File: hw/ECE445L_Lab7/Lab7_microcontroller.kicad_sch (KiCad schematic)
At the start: 12 parts, among them J4 Debugger, SW6 RST, U4 M0G3507QDGS32RQ1, Y1 16MHz

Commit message: work on schem
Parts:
- removed C4: 10nF, ECE445L:C_Radial_100mil, symbol ECE445L:C
- removed R3: 47k, ECE445L:R_Axial_DIN0204_L3.6mm_D1.6mm_P7.62mm_Horizontal, symbol ECE445L:R_0.125W
- removed R7: 100k, ECE445L:R_Axial_DIN0204_L3.6mm_D1.6mm_P7.62mm_Horizontal, symbol ECE445L:R_0.125W
- removed SW6: RST, ECE445L:SW_PUSH_6mm, symbol ECE445L:SW_Push
- added C13, C14: 10pF, Capacitor_SMD:C_0201_0603Metric_Pad0.64x0.40mm_HandSolder, symbol ECE445L:C
- added C_{b,3}: 0.1uF, ECE445L:C_Radial_100mil, symbol ECE445L:C
- added C_{b,4}: 10uF, ECE445L:C_Radial_100mil, symbol ECE445L:C
- added C_{core,2}: 0.47uF, Capacitor_SMD:C_0201_0603Metric_Pad0.64x0.40mm_HandSolder, symbol ECE445L:C
- added J_{flash,2}: Debugger, ECE445L:PinHeader_1x04_P2.54mm_Vertical, symbol ECE445L:Header_4
- added J_{test}: Conn_02x04_Counter_Clockwise, Connector_PinSocket_2.54mm:PinSocket_2x04_P2.54mm_Vertical, symbol Connector_Generic:Conn_02x04_Counter_Clockwise
- added U6: M0G3507QDGS32RQ1, ECE445L:VSSOP_0.5mm_32pin_handsolder, symbol ECE445L:M0G3507QDGS32RQ1
- added Y2: 16MHz, ECE445L:ABM3, symbol ECE445L:ABM3-16.000MHZ-B2-T
- C10, C11: footprint ECE445L:C_Radial_100mil -> Capacitor_SMD:C_0201_0603Metric_Pad0.64x0.40mm_HandSolder
- C_{core,1}: renamed from C9; footprint ECE445L:C_Radial_100mil -> Capacitor_SMD:C_0201_0603Metric_Pad0.64x0.40mm_HandSolder
- renumbered C8 to C_{b,1}, C7 to C_{b,2}, J4 to J_{flash,1}
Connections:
- net +3V3: now also C_{b,3}.1, C_{b,4}.1, J_{flash,2}.4 (C), U6.7 (VDD)
- net GND: now also C13.2, C14.2, C_{b,3}.2, C_{b,4}.2, C_{core,2}.2, J_{flash,2}.3 (C), J_{test}.4 (Pin_4), J_{test}.5 (Pin_5), U6.8 (VSS)
- net PA0 renamed uC_{1} - PA0
- net PA1 renamed uC_{1} - PA1
- net PA10: no longer names the net of U4.17 (PA10/CLK_OUT)
- net PA10: now also U6.16 (PA9/RTC_OUT/CLK_OUT)
- net PA11/SPI0_SCK renamed uC_{1} - PA11
- net PA12 renamed uC_{1} - PA12
- net PA13/TFT_D/C renamed uC_{1} - PA13
- net PA14/SPI0_PICO: no longer names the net of U4.21 (PA14/CLK_OUT/A0_12)
- net PA14/SPI0_PICO: now also U6.11 (PA4/LFCLK_IN/LFXOUT)
- net PA15/DACOUT renamed uC_{1} - PA15
- net PA16/SPI1_POCI renamed uC_{1} - PA16
- net uC_{1} - PA16: now also J_{test}.2 (Pin_2)
- net PA17/SPI1_CLK renamed uC_{1} - PA17
- net PA18/SPI1_PICO renamed uC_{1} - PA18
- net PA2 renamed uC_{1} - PA2
- net PA21 renamed uC_{1} - PA21
- net PA22 renamed uC_{1} - PA22
- net PA23 renamed uC_{1} - PA23
- net PA24/TFT_RESET renamed uC_{1} - PA24
- net PA25/SPI1_CS3 renamed uC_{1} - PA25
- net PA26 renamed uC_{1} - PA26
- net PA27/SPI1_CS1 renamed uC_{1} - PA27
- net uC_{1} - PA27: now also J_{test}.1 (Pin_1)
- net PA3 renamed uC_{1} - PA3
- net PA4 renamed uC_{1} - PA4
- net PA5/HFXIN renamed uC_{1} - HFXIN
- net uC_{1} - HFXIN: now also C13.1, Y2.1
- net PA6/HFXOUT renamed uC_{1} - HFXOUT
- net uC_{1} - HFXOUT: now also C14.1, Y2.2
- net PA7 renamed uC_{1} - PA7
- net PA8/SPI0_CS0 renamed uC_{1} - PA8
- net PA9 renamed uC_{1} - PA9
- net SWCLK: no longer names the net of J_{flash,1}.2 (B), U4.27 (PA20/SWCLK)
- net SWDIO: no longer names the net of J_{flash,1}.1 (A), U4.26 (PA19/SWDIO)
- new net: J_{flash,2}.1 (A), U6.26 (PA19/SWDIO)
- new net: J_{flash,2}.2 (B), U6.27 (PA20/SWCLK)
- new net: C_{core,2}.1, U6.3 (VCORE)
- new net uC_{2} - HFXIN: U6.12 (PA5/HFXIN/FCC_IN)
- new net uC_{2} - HFXOUT: U6.13 (PA6/HFCLK_IN/HFXOUT)
- new net uC_{2} - PA10: U6.17 (PA10/CLK_OUT)
- new net uC_{2} - PA11: U6.18 (PA11)
- new net uC_{2} - PA12: U6.19 (PA12/FCC_IN)
- new net uC_{2} - PA13: U6.20 (PA13)
- new net uC_{2} - PA14: J_{test}.6 (Pin_6), U6.21 (PA14/CLK_OUT/A0_12)
- new net uC_{2} - PA15: U6.22 (PA15/A1_0/DACOUT)
- new net uC_{2} - PA16: U6.23 (PA16/A1_1/FCC_IN)
- new net uC_{2} - PA17: U6.24 (PA17/A1_2)
- new net uC_{2} - PA18: U6.25 (PA18/A1_3)
- new net uC_{2} - PA2: U6.9 (PA2/ROSC)
- new net uC_{2} - PA21: J_{test}.7 (Pin_7), U6.28 (PA21/A1_7/VREF-)
- new net uC_{2} - PA22: J_{test}.8 (Pin_8), U6.29 (PA22/CLK_OUT/A0_7)
- new net uC_{2} - PA23: U6.30 (PA23/VREF+)
- new net uC_{2} - PA24: U6.31 (PA24/A0_3)
- new net uC_{2} - PA25: U6.32 (PA25/A0_2)
- new net uC_{2} - PA26: U6.1 (PA26/A0_1)
- new net uC_{2} - PA27: U6.2 (PA27/RTC_OUT/A0_0)
- new net uC_{2} - PA3: J_{test}.3 (Pin_3), U6.10 (PA3/LFXIN)
- new net uC_{2} - PA7: U6.14 (PA7/CLK_OUT)
- new net uC_{2} - PA8: U6.15 (PA8)
- no-connect marks 0 -> 4
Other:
- note added: "Crystal Oscillators"
- note added: "Master Controller"
- note added: "Oscilloscope/Digital Logic Analyzer/Free Pins"
- note added: "Slave Controller"
- company: (none) -> ECE445L Lab 7
- title: (none) -> MCU
- moved on the sheet: C10, C11, C_{b,1}, C_{b,2}, C_{core,1}, J_{flash,1}, U4, Y1

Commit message: more updates
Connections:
- net uC_{1} - PA0 renamed uC_{1} - KC1
- net uC_{1} - PA1 renamed uC_{1} - KC2
- net uC_{1} - PA11 renamed uC_{1} - KC4
- net uC_{1} - PA3 renamed uC_{1} - KC3
- net uC_{1} - PA4 renamed uC_{1} - KR1
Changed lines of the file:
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@@
 		)
 	)
-	(global_label "uC_{1} - PA1"
+	(global_label "uC_{1} - KC2"
 		(shape output)
 		(at 56.515 84.455 180)
@@
 		)
 		(property "Intersheetrefs" "${INTERSHEET_REFS}"
-			(at 43.0675 84.455 0)
+			(at 42.8861 84.455 0)
 			(hide yes)
 			(show_name no)
@@
 		)
 	)
-	(global_label "uC_{1} - PA3"
+	(global_label "uC_{1} - KC3"
 		(shape output)
 		(at 56.515 97.155 180)
@@
 		)
 		(property "Intersheetrefs" "${INTERSHEET_REFS}"
-			(at 43.0675 97.155 0)
-			(hide yes)
-			(show_name no)
-			(do_not_autoplace no)
-			(effects
-				(font
-					(size 1.27 1.27)
-				)
-				(justify right)
-			)
-		)
-	)
-	(global_label "uC_{1} - PA4"
+			(at 42.8861 97.155 0)
+			(hide yes)
+			(show_name no)
+			(do_not_autoplace no)
+			(effects
+				(font
+					(size 1.27 1.27)
+				)
+				(justify right)
+			)
+		)
+	)
+	(global_label "uC_{1} - KR1"
 		(shape input)
 		(at 56.515 99.695 180)
@@
 		)
 		(property "Intersheetrefs" "${INTERSHEET_REFS}"
-			(at 43.0675 99.695 0)
-			(hide yes)
-			(show_name no)
-			(do_not_autoplace no)
-			(effects
-				(font
-					(size 1.27 1.27)
-				)
-				(justify right)
-			)
-		)
-	)
-	(global_label "uC_{1} - PA11"
+			(at 42.8861 99.695 0)
+			(hide yes)
+			(show_name no)
+			(do_not_autoplace no)
+			(effects
+				(font
+					(size 1.27 1.27)
+				)
+				(justify right)
+			)
+		)
+	)
+	(global_label "uC_{1} - KC4"
 		(shape output)
 		(at 112.395 109.855 0)
@@
 		)
 		(property "Intersheetrefs" "${INTERSHEET_REFS}"
-			(at 127.052 109.855 0)
+			(at 126.0239 109.855 0)
 			(hide yes)
 			(show_name no)
@@
 		)
 	)
-	(global_label "uC_{1} - PA0"
+	(global_label "uC_{1} - KC1"
 		(shape output)
 		(at 56.515 81.915 180)
@@
 		)
 		(property "Intersheetrefs" "${INTERSHEET_REFS}"
-			(at 43.0675 81.915 0)
-			(hide yes)
-			(show_name no)
+			(at 42.8861 81.915 0)
+			(hide yes)
+			(show_name no)

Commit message: mostly finished schem
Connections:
- net GND: now also J_{test}.3 (Pin_3)
- net uC_{1} - PA25: now also J_{test}.1 (Pin_1)
- net uC_{1} - PA27: no longer J_{test}.1 (Pin_1)
- net uC_{2} - PA21: no longer J_{test}.7 (Pin_7)
- net uC_{2} - PA3: now also J_{test}.7 (Pin_7), J_{test}.8 (Pin_8); no longer J_{test}.3 (Pin_3)
- net uC_{1} - PA23 renamed uC_{1} - KR3
- net uC_{1} - PA26 renamed uC_{1} - KR4
- net uC_{1} - PA7 renamed uC_{1} - KR2
- net uC_{2} - PA10 renamed uC_{2} - Motor_{4}
- net uC_{2} - PA12 renamed uC_{2} - Solenoid
- net uC_{2} - PA15 renamed uC_{2} - Speaker
- net uC_{2} - PA22 renamed uC_{2} - Flywheels
- net uC_{2} - Flywheels: no longer J_{test}.8 (Pin_8)
- net uC_{2} - PA23 renamed uC_{2} - Motor_{2}
- net uC_{2} - PA26 renamed uC_{2} - Motor_{1}
- net uC_{2} - PA8 renamed uC_{2} - Motor_{3}
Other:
- moved on the sheet: C10, C11, C13, C14, J_{flash,2}, J_{test}, Y1, Y2

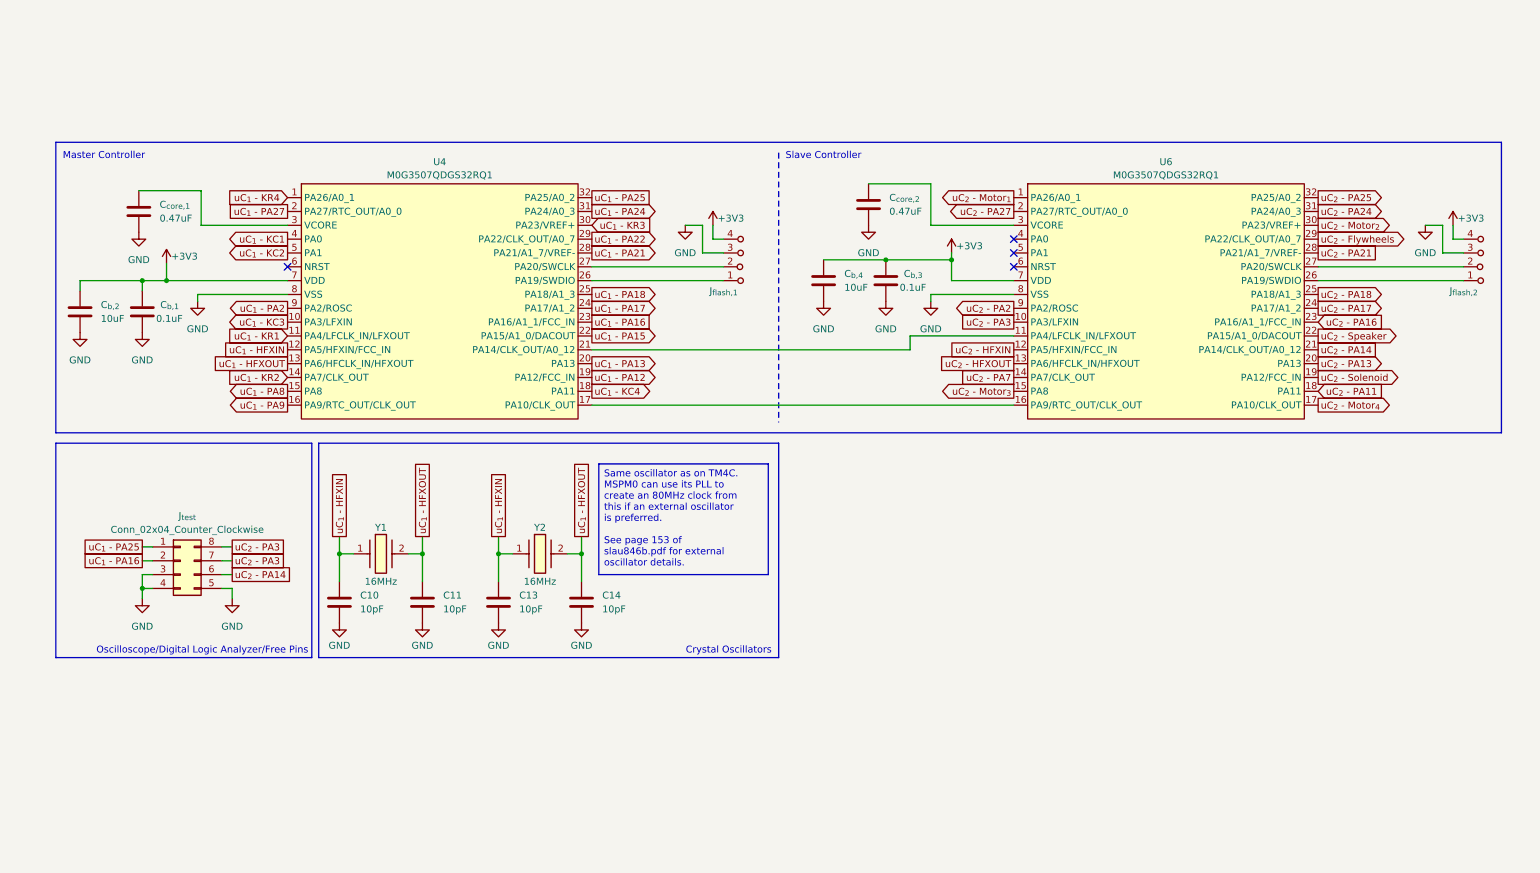
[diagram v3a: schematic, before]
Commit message: added reverse engineering for water atomizer
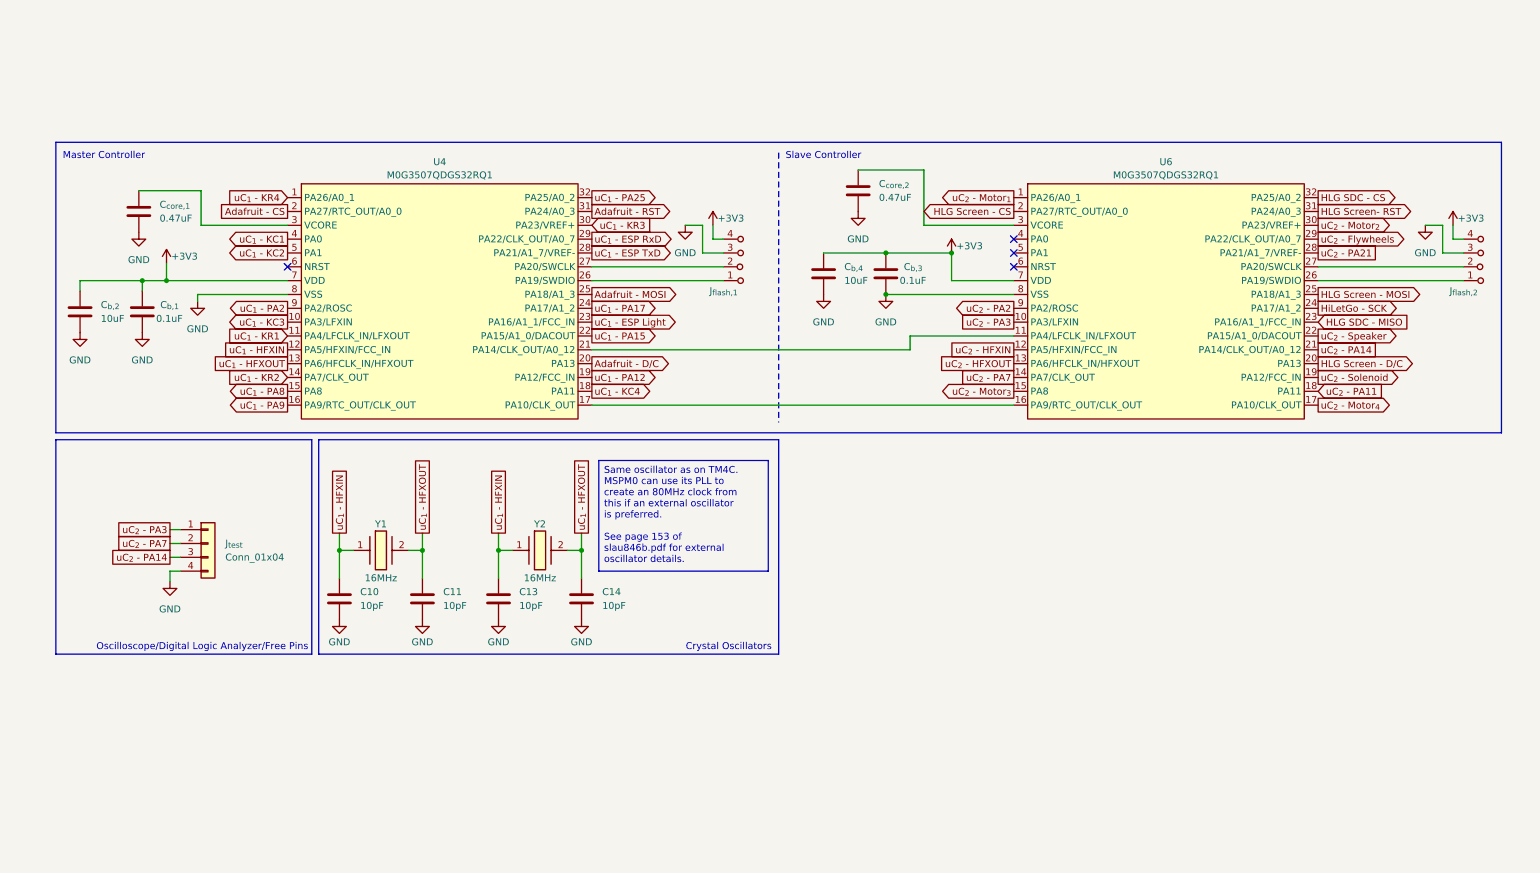
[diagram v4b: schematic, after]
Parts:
- removed J_{test}: Conn_02x04_Counter_Clockwise, Connector_PinSocket_2.54mm:PinSocket_2x04_P2.54mm_Vertical, symbol Connector_Generic:Conn_02x04_Counter_Clockwise
- added J_{test}: Conn_01x04, Connector_PinHeader_2.54mm:PinHeader_1x04_P2.54mm_Vertical, symbol Connector_Generic:Conn_01x04
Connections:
- net GND: now also J_{test}.4 (Pin_4)
- net uC_{2} - PA14: now also J_{test}.3 (Pin_3)
- net uC_{2} - PA3: now also J_{test}.1 (Pin_1)
- net uC_{2} - PA7: now also J_{test}.2 (Pin_2)
- net uC_{1} - PA13 renamed Adafruit - D/C
- net uC_{1} - PA16 renamed uC_{1} - ESP Light
- net uC_{1} - PA18 renamed Adafruit - MOSI
- net uC_{1} - PA21 renamed uC_{1} - ESP TxD
- net uC_{1} - PA22 renamed uC_{1} - ESP RxD
- net uC_{1} - PA24 renamed Adafruit - RST
- net uC_{1} - PA27 renamed Adafruit - CS
- net uC_{2} - PA13 renamed HLG Screen - D/C
- net uC_{2} - PA16 renamed HLG SDC - MISO
- net uC_{2} - PA17 renamed HiLetGo - SCK
- net uC_{2} - PA18 renamed HLG Screen - MOSI
- net uC_{2} - PA24 renamed HLG Screen- RST
- net uC_{2} - PA25 renamed HLG SDC - CS
- net uC_{2} - PA27 renamed HLG Screen - CS
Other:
- company: ECE445L Lab 7 -> ECE445L
- moved on the sheet: C10, C11, C13, C14, C_{b,3}, C_{b,4}, C_{core,2}, Y1, Y2

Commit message: almost finished with schem
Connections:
- net uC_{2} - PA11 is gone; now on net uC SPI - SCK: U6.18 (PA11)
- net uC_{2} - PA2 is gone; now on net uC SPI - CS: U6.9 (PA2/ROSC)
- net uC_{1} - SWDIO: now reaches J_{flash,1}.1 (A), U4.26 (PA19/SWDIO)
- net uC_{1} - SWCLK: now reaches J_{flash,1}.2 (B), U4.27 (PA20/SWCLK)
- net uC_{1} - V_{core}: now reaches C_{core,1}.1, U4.3 (VCORE)
- net uC_{2} - SWDIO: now reaches J_{flash,2}.1 (A), U6.26 (PA19/SWDIO)
- net uC_{2} - SWCLK: now reaches J_{flash,2}.2 (B), U6.27 (PA20/SWCLK)
- net uC_{2} - V_{core}: now reaches C_{core,2}.1, U6.3 (VCORE)
- net uC SPI - uC_{1} -> uC_{2}: now reaches U4.21 (PA14/CLK_OUT/A0_12), U6.11 (PA4/LFCLK_IN/LFXOUT)
- net uC SPI - uC_{1} <- uC_{2}: now reaches U4.17 (PA10/CLK_OUT), U6.16 (PA9/RTC_OUT/CLK_OUT)
- net uC_{2} - Smoke: now reaches U6.5 (PA1)
- net uC_{1} - KC1 renamed Keypad - C1
- net uC_{1} - KC2 renamed Keypad - C2
- net uC_{1} - KC3 renamed Keypad - C3
- net uC_{1} - KC4 renamed Keypad - C4
- net uC_{1} - KR1 renamed Keypad - R1
- net uC_{1} - KR2 renamed Keypad - R2
- net uC_{1} - KR3 renamed Keypad - R3
- net uC_{1} - KR4 renamed Keypad - R4
- net uC_{1} - PA12 renamed uC SPI - SCK
- net uC_{1} - PA2 renamed uC SPI - CS
- net uC_{1} - PA25 renamed uC_{1} - ESP RST
- net uC_{1} - PA8 renamed ID Scan - TxD
- net uC_{1} - PA9 renamed ID Scan - RxD
- net uC_{2} - Motor_{1} renamed uC_{2} - Motor _{1}
- net uC_{2} - Motor_{2} renamed uC_{2} - Motor _{2}
- net uC_{2} - Motor_{3} renamed uC_{2} - Motor _{3}
- net uC_{2} - Motor_{4} renamed uC_{2} - Motor _{4}
- no-connect marks 4 -> 3
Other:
- moved on the sheet: C_{b,3}, C_{b,4}, C_{core,2}, J_{flash,1}

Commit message: finished prelim schem
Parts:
- removed J_{test}: Conn_01x04, Connector_PinHeader_2.54mm:PinHeader_1x04_P2.54mm_Vertical, symbol Connector_Generic:Conn_01x04
- added J_{test}1: Conn_02x04_Counter_Clockwise, Connector_PinSocket_2.54mm:PinSocket_2x04_P2.54mm_Vertical, symbol Connector_Generic:Conn_02x04_Odd_Even
- added SPI_{CS}1, SPI_{SCK}1, uC_{1}←uC_{2}1, uC_{1}→uC_{2}1: TestPoint, TestPoint:TestPoint_Keystone_5010-5014_Multipurpose, symbol Connector:TestPoint
- C_{b,uC}1: renamed from C_{b,1}; value 0.1uF -> 100n; footprint ECE445L:C_Radial_100mil -> Capacitor_SMD:C_0603_1608Metric_Pad1.08x0.95mm_HandSolder; Distributor (none) -> Mouser; Manufacturer (none) -> Walsin; Manufacturer_Part_Number (none) -> 0603B104J160CT; Mouser Part Number (none) -> 791-0603B104J160CT
- C_{b,uC}2: renamed from C_{b,2}; value 10uF -> 10u; footprint ECE445L:C_Radial_100mil -> Capacitor_SMD:C_0603_1608Metric_Pad1.08x0.95mm_HandSolder; Distributor (none) -> Mouser; Manufacturer (none) -> TDK; Manufacturer_Part_Number (none) -> C1608X7T1A106M080AC; Mouser Part Number (none) -> 810-C1608X7T1A106M08
- C_{b,uC}3: renamed from C_{b,3}; value 0.1uF -> 100n; footprint ECE445L:C_Radial_100mil -> Capacitor_SMD:C_0603_1608Metric_Pad1.08x0.95mm_HandSolder; Distributor (none) -> Mouser; Manufacturer (none) -> Walsin; Manufacturer_Part_Number (none) -> 0603B104J160CT; Mouser Part Number (none) -> 791-0603B104J160CT
- C_{b,uC}4: renamed from C_{b,4}; value 10uF -> 10u; footprint ECE445L:C_Radial_100mil -> Capacitor_SMD:C_0603_1608Metric_Pad1.08x0.95mm_HandSolder; Distributor (none) -> Mouser; Manufacturer (none) -> TDK; Manufacturer_Part_Number (none) -> C1608X7T1A106M080AC; Mouser Part Number (none) -> 810-C1608X7T1A106M08
- C_{core}1: renamed from C_{core,1}; value 0.47uF -> 0.47u; footprint Capacitor_SMD:C_0201_0603Metric_Pad0.64x0.40mm_HandSolder -> Capacitor_SMD:C_0603_1608Metric_Pad1.08x0.95mm_HandSolder; Distributor (none) -> Mouser; Manufacturer (none) -> Walsin; Manufacturer_Part_Number (none) -> 0603B474K6R3CT; Mouser Part Number (none) -> 791-0603B474K6R3CT
- C_{core}2: renamed from C_{core,2}; value 0.47uF -> 0.47u; footprint Capacitor_SMD:C_0201_0603Metric_Pad0.64x0.40mm_HandSolder -> Capacitor_SMD:C_0603_1608Metric_Pad1.08x0.95mm_HandSolder; Distributor (none) -> Mouser; Manufacturer (none) -> Walsin; Manufacturer_Part_Number (none) -> 0603B474K6R3CT; Mouser Part Number (none) -> 791-0603B474K6R3CT
- C_{y}1: renamed from C10; value 10pF -> 10p; footprint Capacitor_SMD:C_0201_0603Metric_Pad0.64x0.40mm_HandSolder -> Capacitor_SMD:C_0603_1608Metric_Pad1.08x0.95mm_HandSolder; Distributor (none) -> Mouser; Manufacturer (none) -> Walsin; Manufacturer_Part_Number (none) -> 0603N100F101CT; Mouser Part Number (none) -> 791-0603N100F101CT
- C_{y}2: renamed from C11; value 10pF -> 10p; footprint Capacitor_SMD:C_0201_0603Metric_Pad0.64x0.40mm_HandSolder -> Capacitor_SMD:C_0603_1608Metric_Pad1.08x0.95mm_HandSolder; Distributor (none) -> Mouser; Manufacturer (none) -> Walsin; Manufacturer_Part_Number (none) -> 0603N100F101CT; Mouser Part Number (none) -> 791-0603N100F101CT
- C_{y}3: renamed from C13; value 10pF -> 10p; footprint Capacitor_SMD:C_0201_0603Metric_Pad0.64x0.40mm_HandSolder -> Capacitor_SMD:C_0603_1608Metric_Pad1.08x0.95mm_HandSolder; Distributor (none) -> Mouser; Manufacturer (none) -> Walsin; Manufacturer_Part_Number (none) -> 0603N100F101CT; Mouser Part Number (none) -> 791-0603N100F101CT
- C_{y}4: renamed from C14; value 10pF -> 10p; footprint Capacitor_SMD:C_0201_0603Metric_Pad0.64x0.40mm_HandSolder -> Capacitor_SMD:C_0603_1608Metric_Pad1.08x0.95mm_HandSolder; Distributor (none) -> Mouser; Manufacturer (none) -> Walsin; Manufacturer_Part_Number (none) -> 0603N100F101CT; Mouser Part Number (none) -> 791-0603N100F101CT
- Y1, Y2: Manufacturer (none) -> ABRACON
- renumbered J_{flash,1} to J_{flash}1, J_{flash,2} to J_{flash}2, U4 to uC1, U6 to uC2
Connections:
- net GND: now also J_{test}1.2 (Pin_2), J_{test}1.4 (Pin_4), J_{test}1.6 (Pin_6), J_{test}1.8 (Pin_8)
- net uC SPI - CS: now also SPI_{CS}1.1
- net uC SPI - SCK: now also SPI_{SCK}1.1
- net uC_{1} - HFXIN: no longer C_{y}3.1, Y2.1
- net uC_{1} - HFXOUT: no longer C_{y}4.1, Y2.2
- net uC_{2} - HFXIN: now also C_{y}3.1, Y2.1
- net uC_{2} - HFXOUT: now also C_{y}4.1, Y2.2
- net Motor PWM: now reaches uC2.4 (PA0)
- net uC SPI - uC_{1} -> uC_{2} renamed uC SPI - uC_{1} → uC_{2}
- net uC SPI - uC_{1} → uC_{2}: now also uC_{1}→uC_{2}1.1
- net uC SPI - uC_{1} <- uC_{2} renamed uC SPI - uC_{1} ← uC_{2}
- net uC SPI - uC_{1} ← uC_{2}: now also uC_{1}←uC_{2}1.1
- net uC_{1} - PA15 renamed uC_{1} - Speaker
- net uC_{1} - PA17 renamed Adafruit - SCK
- net uC_{2} - Flywheels renamed Flywheels
- net uC_{2} - Motor _{1} renamed uC_{2} - Motor_{1}
- net uC_{2} - Motor _{2} renamed uC_{2} - Motor_{2}
- net uC_{2} - Motor _{3} renamed uC_{2} - Motor_{3}
- net uC_{2} - Motor _{4} renamed uC_{2} - Motor_{4}
- net uC_{2} - PA14 renamed PA14/LG3
- net PA14/LG3: now also J_{test}1.5 (Pin_5)
- net uC_{2} - PA21 renamed PA21/LG4
- net PA21/LG4: now also J_{test}1.7 (Pin_7)
- net uC_{2} - PA3 renamed PA3/LG1
- net PA3/LG1: now also J_{test}1.1 (Pin_1)
- net uC_{2} - PA7 renamed PA7/LG2
- net PA7/LG2: now also J_{test}1.3 (Pin_3)
- net uC_{2} - Smoke renamed Smoke
- net uC_{2} - Solenoid renamed Solenoid
- no-connect marks 3 -> 2
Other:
- note added: "Test Points"
- note removed: "Oscilloscope/Digital Logic Analyzer/Free Pins"
- moved on the sheet: C_{b,uC}1, C_{b,uC}2, C_{b,uC}3, C_{b,uC}4, C_{core}1, C_{core}2, C_{y}1, C_{y}2, C_{y}3, C_{y}4, J_{flash}1, J_{flash}2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
